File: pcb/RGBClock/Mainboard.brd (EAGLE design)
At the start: 100 x 80 mm, 89 parts, among them IC1 MCP23017SO, K1 G6K-2F, K2 G6K-2F, K3 G6K-2F, K4 G6K-2F, Q1 32.768KHz, Q2 32.768KHz, U10 NX3L1G384GW, U11 NX3L1G384GW, U12 NX3L1G384GW, U13 DRV612PW, U14 2N7002-7-F, U15 2N7002-7-F, U16 2N7002-7-F, U17 2N7002-7-F, U2 MAX6369KA+T, U3 TXS0102DCUR, U4 P82B96DR, U5 LM2675M-5.0, U6 DS1338Z-33+, U7 SI4735-D50, U8 TPS71533DCKR, U9 NX3L1G384GW, X3 1503_09, X4 1503_09, X5 43045-0400, X6 43045-0800

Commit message: Cleanup schematic
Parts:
- removed U17: 2N7002-7-F, Diodes:SOT103P240X110-3N
- removed X6: 43045-0800, con-molex-micro-fit-3_0:43045-0800
- added U1: MAX6369KA+T, Maxim_By_element14_Batch_1:SOT65P280X145-8N
- added X2: 43045-0400, con-molex-micro-fit-3_0:43045-0400
- D11: value CDSOD323-T03C -> 1N4148DO35-7; device MyComponents:SOD323 -> diode:DO35-7
- D7: value 1N4148DO35-7 -> CDSOD323-T03C; device diode:DO35-7 -> MyComponents:SOD323
- U12: value NX3L1G384GW -> DRV612PW; device NXP_By_element14_Batch_1:SOT65P212X110-5N -> Texas:SOP65P640X120-14N
- U13: value DRV612PW -> 2N7002-7-F; device Texas:SOP65P640X120-14N -> Diodes:SOT103P240X110-3N
- U2: value MAX6369KA+T -> TXS0102DCUR; device Maxim_By_element14_Batch_1:SOT65P280X145-8N -> Texas:SOP50P310X90-8N
- U3: value TXS0102DCUR -> P82B96DR; device Texas:SOP50P310X90-8N -> Texas:SOIC127P600X175-8N
- U4: value P82B96DR -> LM2675M-5.0; device Texas:SOIC127P600X175-8N -> Texas:SOIC127P620X175-8N
- U5: value LM2675M-5.0 -> DS1338Z-33+; device Texas:SOIC127P620X175-8N -> Maxim_By_element14_Batch_1:SOIC127P600X175-8N
- U6: value DS1338Z-33+ -> SI4735-D50; device Maxim_By_element14_Batch_1:SOIC127P600X175-8N -> SiliconLabs:SSOP24
- U7: value SI4735-D50 -> TPS71533DCKR; device SiliconLabs:SSOP24 -> Texas:SOT65P210X110-5N
- U8: value TPS71533DCKR -> NX3L1G384GW; device Texas:SOT65P210X110-5N -> NXP_By_element14_Batch_1:SOT65P212X110-5N
- X5: value 43045-0400 -> 43045-0800; device con-molex-micro-fit-3_0:43045-0400 -> con-molex-micro-fit-3_0:43045-0800
- moved X5 92.5 mm to (97.3, 66.8), turned to 90 degrees
- moved U5 70.3 mm to (36.6, 3.56), turned to 0 degrees
- moved D7 58.0 mm to (24.6, 48.5), turned to 0 degrees
- moved U7 52.7 mm to (30.0, 59.9)
- moved U4 50.9 mm to (55.1, 71.4), turned to 90 degrees
- moved U8 49.3 mm to (58.2, 19.6), turned to 0 degrees
- moved D11 47.4 mm to (71.4, 52.1), turned to 180 degrees
- moved U12 42.3 mm to (89.2, 24.6), turned to 270 degrees
- moved D5 37.4 mm to (43.9, 13.5)
- moved U13 35.4 mm to (63.5, 49.0), turned to 0 degrees
- moved U6 20.2 mm to (54.4, 13.2), turned to 180 degrees
- moved U10 17.4 mm to (58.7, 3.30)
- moved D10 13.7 mm to (71.1, 65.8)
- moved D8 13.7 mm to (82.5, 52.1)
- moved U3 12.2 mm to (17.8, 36.8)
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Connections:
- net +3V3: now also U1.4, U1.5, U1.6, U1.8, U12.10, U2.7, U3.8, U5.7, U6.16, U6.20, U6.21, U7.5; no longer U12.5, U13.10, U2.4, U2.5, U2.6, U2.8, U3.7, U4.8, U6.7, U7.16, U7.20, U7.21
- net +5V: now also U4.4, U7.4; no longer U5.4, U8.4
- net GND: now also D7.P$1, U1.2, U12.11, U13.2, U3.4, U4.6, U5.4, U6.13, U6.14, U6.9, U7.2, U8.3, X2.P$1; no longer D11.P$1, U13.11, U13.3, U17.2, U3.2, U4.4, U5.6, U6.4, U7.13, U7.14, U7.9, U8.2, X5.P$1
- net N$1: now also X2.P$2; no longer X5.P$2
- net N$10: now also U4.1; no longer U5.1
- net N$11: now also U4.8; no longer U5.8
- net N$12: now also X5.P$7; no longer X6.P$7
- net N$13: now also X5.P$8; no longer X6.P$8
- net N$14: now also U2.8, U3.1; no longer U3.8, U4.1
- net N$15: now also U5.2; no longer U6.2
- net N$16: now also U5.3; no longer U6.3
- net N$17: now also U5.1; no longer U6.1
- net N$18: now also U13.1; no longer U14.1
- net N$19: now also U14.1; no longer U15.1
- net N$20: now also X5.P$2; no longer X6.P$2
- net N$21: now also U15.1; no longer U16.1
- net N$22: now also D8.A, U13.3; no longer D7.A, U14.3
- net N$23: now also D9.A, U14.3; no longer D8.A, U15.3
- net N$24: now also D10.A, U15.3; no longer D9.A, U16.3
- net N$25: now also U6.3; no longer U7.3
- net N$26: now also U6.19; no longer U7.19
- net N$27: now also U6.24, U8.1; no longer U7.24, U9.1
- net N$28: now also U6.23, U9.1; no longer U10.1, U7.23
- net N$29: now also U10.2, U8.2; no longer U11.2, U9.2
- net N$3: now also U2.5; no longer U3.5
- net N$30: now also U11.2, U9.2; no longer U10.2, U12.2
- net N$31: now also U10.4; no longer U12.4
- net N$33: now also U1.1; no longer U2.1
- net N$35: now also U6.15; no longer U7.15
- net N$36: now also D7.P$2, U11.1; no longer D6.P$2, U12.1
- net N$37: now also D6.P$2, U10.1; no longer D5.P$2, U11.1
- net N$38: now also U12.4; no longer U13.4
- net N$4: now also U5.5, U6.18; no longer U6.5, U7.18
- net N$40: now also U12.2; no longer U13.2
- net N$44: now also U12.13; no longer U13.13
- net N$46: now also U12.12; no longer U13.12
- net N$5: now also X5.P$1; no longer X6.P$1
- net N$51: now also U1.7; no longer U2.7
- net N$52: now also X5.P$3; no longer X6.P$3
- net N$53: now also U12.1; no longer U13.1
- net N$54: now also U12.9; no longer U13.9
- net N$55: now also U12.14; no longer U13.14
- net N$56: now also U12.6; no longer U13.6
- net N$57: now also U12.5; no longer U13.5
- net N$59: now also D5.P$2, U6.8; no longer D11.P$2, U7.8
- net N$6: now also U2.4; no longer U3.4
- net N$60: now also X5.P$4; no longer X6.P$4
- net N$61: now also U6.22; no longer U7.22
- net N$62: now also U5.6, U6.17; no longer U6.6, U7.17
- net N$63: now also X5.P$5; no longer X6.P$5
- net N$64: now also X5.P$6; no longer X6.P$6
- net N$65: now also U2.1, U3.7; no longer U3.1, U4.7
- net N$66: now also U8.4; no longer U10.4
- net N$7: now also U16.1; no longer U17.1
- net N$8: now also U2.3, U2.6; no longer U3.3, U3.6
- net N$9: now also D11.A, U16.3; no longer D10.A, U17.3
- net SCL_LONG: now also U3.5, U3.6, X2.P$4; no longer U4.5, U4.6, X5.P$4
- net SDA_LONG: now also U3.2, U3.3, X2.P$3; no longer U4.2, U4.3, X5.P$3
- net VCC: now also D11.C, U4.7; no longer D7.C, U5.7

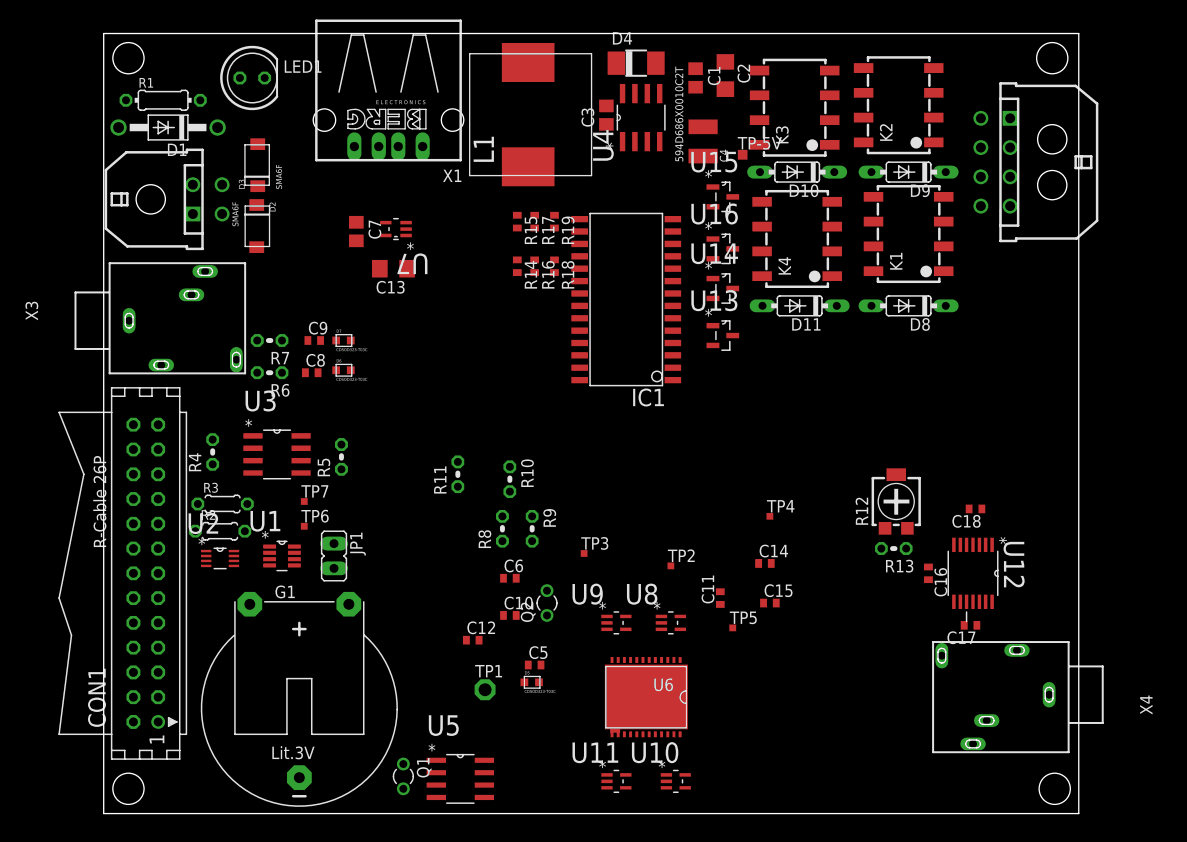
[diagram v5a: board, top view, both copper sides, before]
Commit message: 
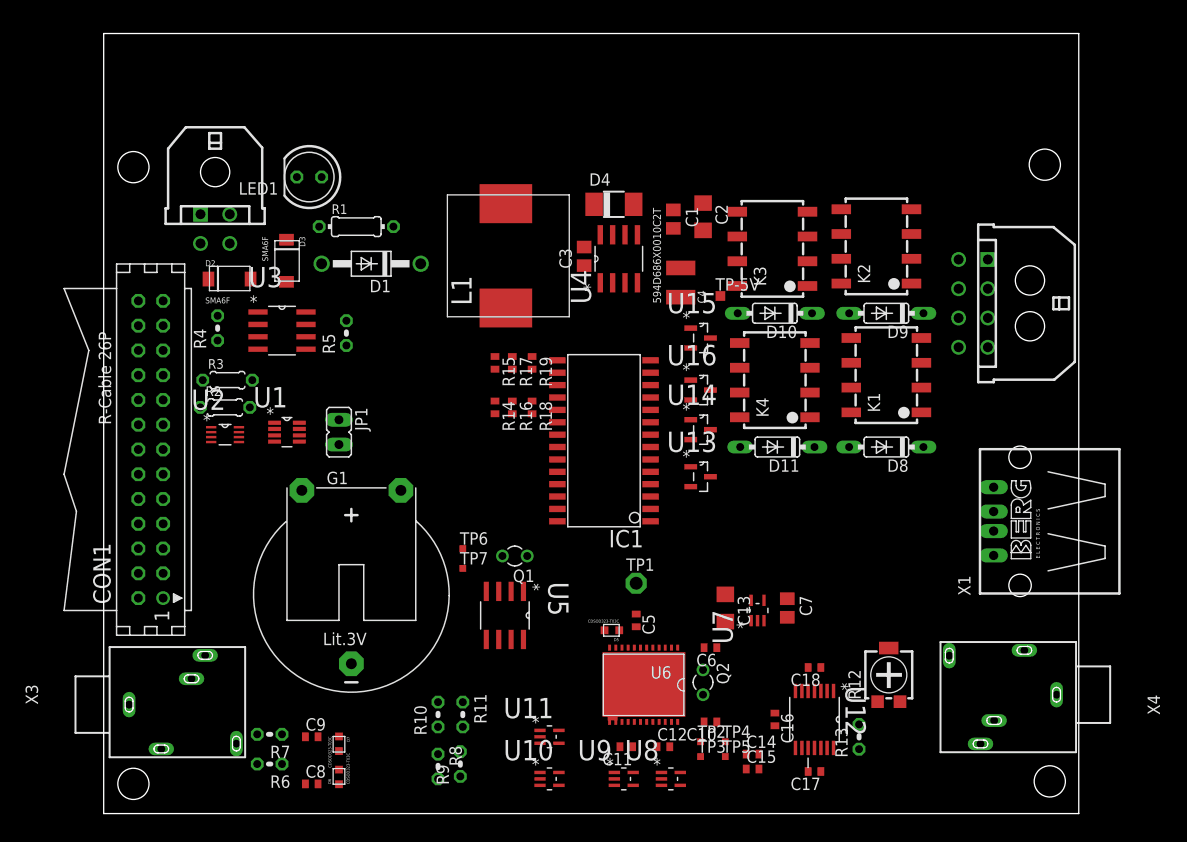
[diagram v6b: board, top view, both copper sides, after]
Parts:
- moved X1 76.7 mm to (94.0, 30.0), turned to 90 degrees
- moved C7 58.7 mm to (70.1, 21.1)
- moved U7 53.9 mm to (67.1, 20.8), turned to 90 degrees
- moved C13 48.7 mm to (63.8, 21.1), turned to 270 degrees
- moved C8 42.2 mm to (21.3, 3.05)
- moved D6 41.7 mm to (24.1, 3.81), turned to 90 degrees
- moved D7 41.4 mm to (24.1, 7.11), turned to 270 degrees
- moved C9 40.6 mm to (21.3, 7.87)
- moved R7 40.4 mm to (17.0, 8.13)
- moved R6 40.1 mm to (17.0, 5.08)
- moved X3 39.4 mm to (0.51, 11.2)
- moved Q1 25.3 mm to (42.2, 26.4), turned to 180 degrees
- moved R8 25.3 mm to (34.3, 4.83), turned to 270 degrees
- moved R9 25.2 mm to (36.6, 5.08), turned to 90 degrees
- moved R10 25.2 mm to (34.3, 10.2), turned to 90 degrees
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
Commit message: Beta version master pcb (not complete routed !)
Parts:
- removed TP1: PTR1PAD1-13, testpad:P1-13
- added ANT: PTR1PAD1-13, testpad:P1-13
- moved TP-5V 27.6 mm to (66.3, 25.7)
- moved TP6 5.84 mm to (36.8, 33.0)
- moved TP7 5.08 mm to (36.8, 30.2)
- moved LED1 4.13 mm to (25.1, 66.0)
- moved U13 3.56 mm to (61.2, 31.0)
- moved U14 3.05 mm to (61.2, 36.3)
- moved U15 2.03 mm to (61.2, 46.7)
- moved U16 1.78 mm to (61.2, 41.7)
- moved K2 1.30 mm to (80.5, 58.4)
- moved D4 1.27 mm to (53.6, 62.5)
- moved U4 1.02 mm to (53.8, 56.9)
- moved TP3 0.80 mm to (61.5, 5.08)
- moved TP5 0.80 mm to (63.5, 5.08)
- moved K3 0.57 mm to (68.8, 58.4)
- moved C3 0.57 mm to (49.8, 56.9)
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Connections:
- net N$58: now also ANT.TP; no longer TP1.TP
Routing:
- net +3V3: track 0.00 -> 229.1 mm, vias 0 -> 3
- net VCC: track 0.00 -> 139.0 mm
- net +5V: track 0.00 -> 88.5 mm
- net N$4: track 0.00 -> 64.4 mm, vias 0 -> 2
- net N$33: track 0.00 -> 63.7 mm, vias 0 -> 2
- net N$62: track 0.00 -> 60.2 mm, vias 0 -> 2
- net N$66: track 0.00 -> 45.8 mm, vias 0 -> 2
- net N$60: track 0.00 -> 37.1 mm
- net N$36: track 0.00 -> 37.0 mm
- net N$31: track 0.00 -> 36.9 mm, vias 0 -> 2
- net SCL_LONG: track 0.00 -> 34.7 mm
- net N$30: track 0.00 -> 34.4 mm, vias 0 -> 3
- net N$29: track 0.00 -> 32.8 mm, vias 0 -> 2
- net N$38: track 0.00 -> 31.4 mm, vias 0 -> 2
- net N$23: track 0.00 -> 29.2 mm, vias 0 -> 2
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- added copper zone on layer 1, net GND
- added copper zone on layer 16, net GND
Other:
- board size 100 x 80 mm -> 99.8 x 70.1 mm

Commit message: Just before freerouter
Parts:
- moved TP-5V 3.86 mm to (70.1, 25.0)
- moved JP1 3.86 mm to (27.9, 39.8)
- moved K2 3.17 mm to (80.5, 61.6)
- moved K3 3.17 mm to (68.8, 61.6)
- moved R14 3.17 mm to (37.0, 41.7)
- moved R15 3.17 mm to (37.0, 46.2)
- moved R16 3.17 mm to (38.7, 41.7)
- moved R17 3.17 mm to (38.7, 46.2)
- moved R18 3.17 mm to (40.8, 41.7)
- moved R19 3.17 mm to (40.8, 46.2)
- moved D10 3.11 mm to (69.2, 54.6)
- moved D9 3.09 mm to (80.0, 54.6)
- moved U2 2.29 mm to (13.7, 37.0)
- moved U1 2.01 mm to (20.7, 39.8)
- moved U10 1.91 mm to (43.8, 3.56)
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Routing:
- net +3V3: track 229.1 -> 0.00 mm, vias 3 -> 0
- net VCC: track 139.0 -> 0.00 mm
- net +5V: track 88.5 -> 0.00 mm
- net N$4: track 64.4 -> 0.00 mm, vias 2 -> 0
- net N$33: track 63.7 -> 0.00 mm, vias 2 -> 0
- net N$62: track 60.2 -> 0.00 mm, vias 2 -> 0
- net N$66: track 45.8 -> 0.00 mm, vias 2 -> 0
- net N$60: track 37.1 -> 0.00 mm
- net N$36: track 37.0 -> 0.00 mm
- net N$31: track 36.9 -> 0.00 mm, vias 2 -> 0
- net SCL_LONG: track 34.7 -> 0.00 mm
- net N$30: track 34.4 -> 0.00 mm, vias 3 -> 0
- net N$29: track 32.8 -> 0.00 mm, vias 2 -> 0
- net N$38: track 31.4 -> 0.00 mm, vias 2 -> 0
- net N$23: track 29.2 -> 0.00 mm, vias 2 -> 0
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- removed copper zone on layer 1, net GND
- removed copper zone on layer 16, net GND
